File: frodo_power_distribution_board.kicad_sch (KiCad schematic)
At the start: 3 parts, among them J1 Payload_1, J2 Payload_2, J3 Payload_3

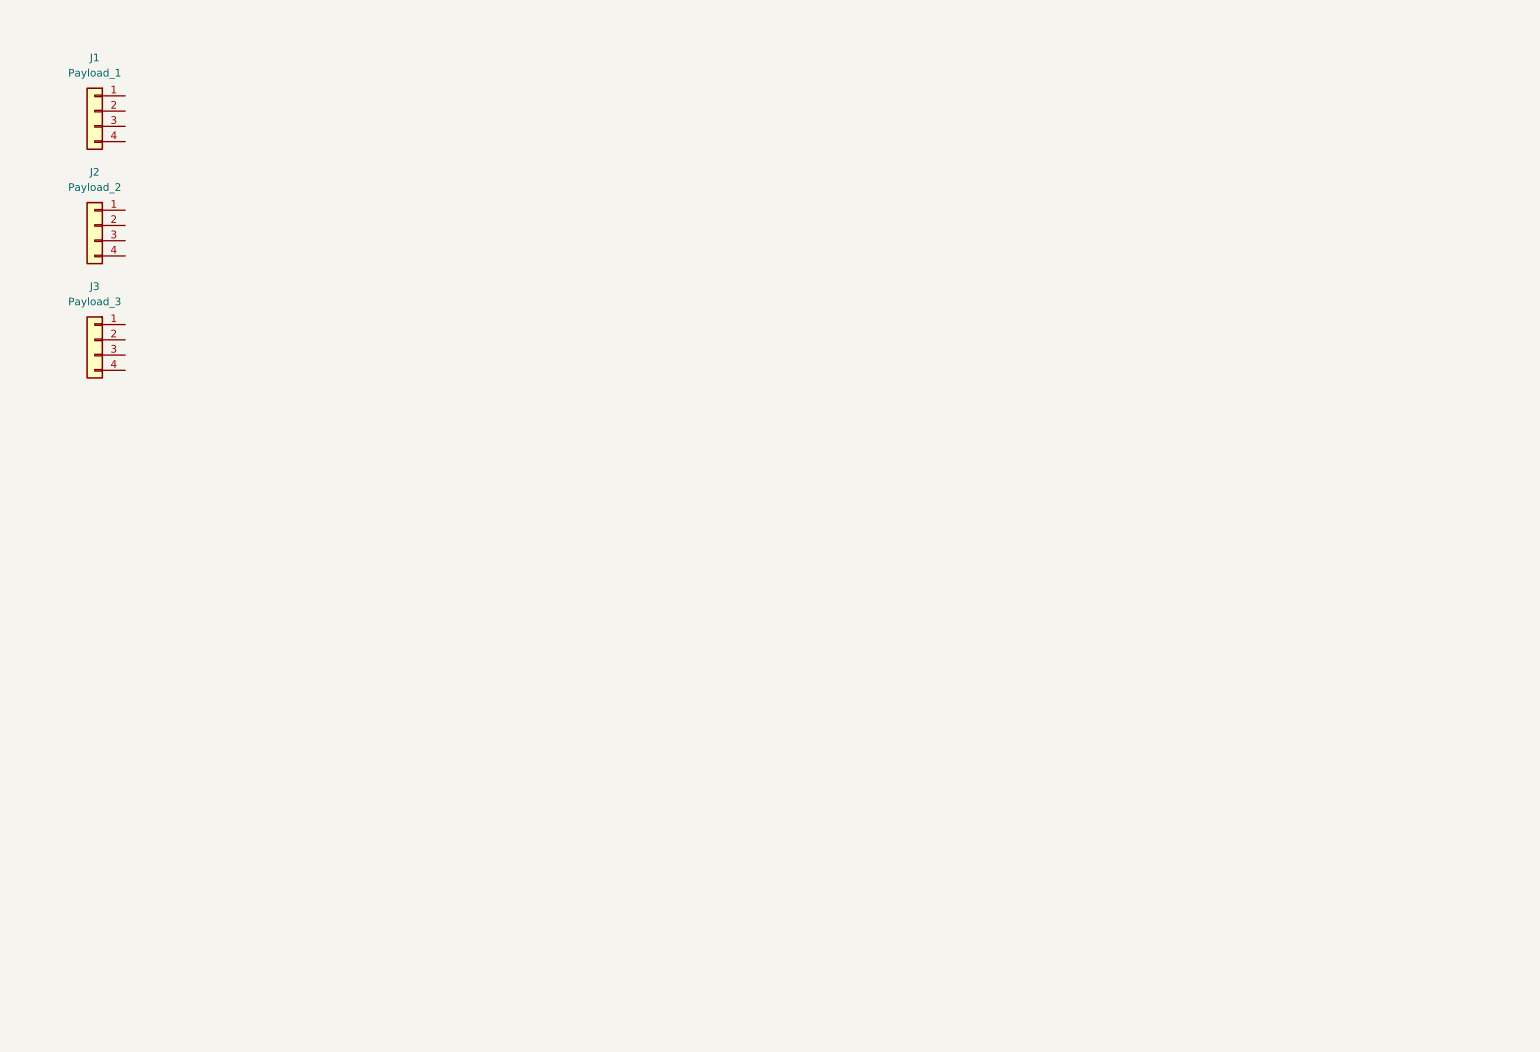
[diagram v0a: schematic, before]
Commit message: Specify board schematics
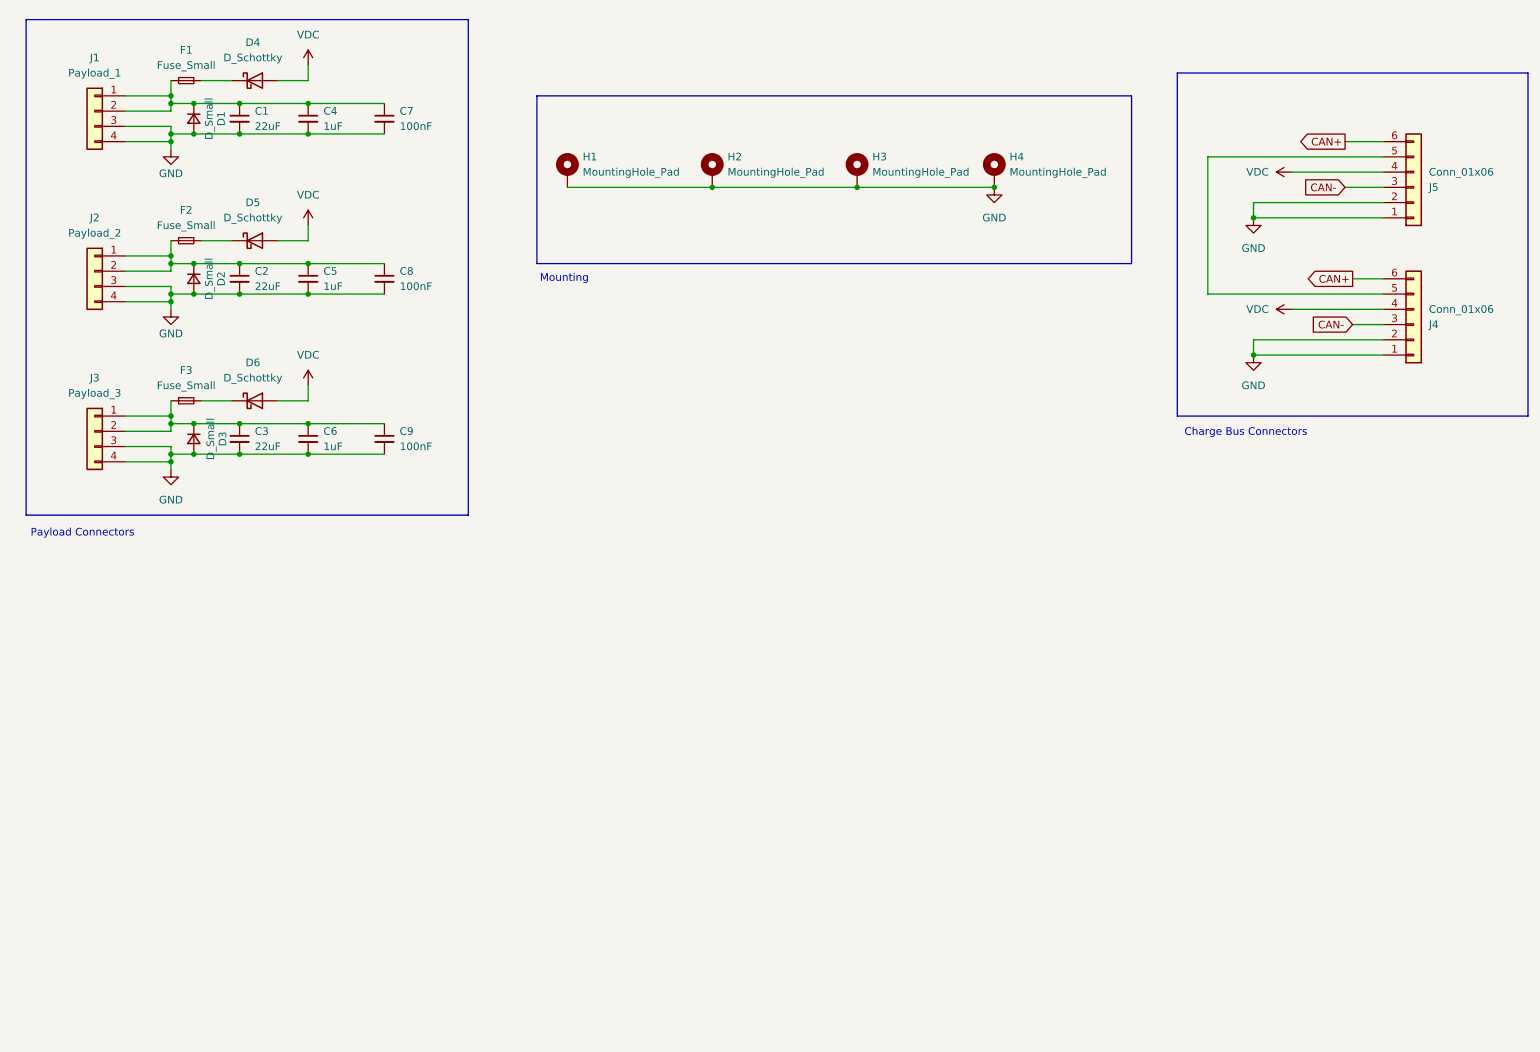
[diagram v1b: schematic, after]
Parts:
- added C1, C2, C3: 22uF, Capacitor_SMD:C_1206_3216Metric_Pad1.33x1.80mm_HandSolder, symbol Device:C_Small
- added C4, C5, C6: 1uF, Capacitor_SMD:C_0805_2012Metric_Pad1.18x1.45mm_HandSolder, symbol Device:C_Small
- added C7, C8, C9: 100nF, Capacitor_SMD:C_0603_1608Metric_Pad1.08x0.95mm_HandSolder, symbol Device:C_Small
- added D1, D2, D3: D_Small, Diode_SMD:D_SOD-123F, symbol Device:D_Small
- added D4, D5, D6: D_Schottky, Diode_SMD:D_SMA, symbol Device:D_Schottky
- added F1, F2, F3: Fuse_Small, Fuse:Fuse_1206_3216Metric, symbol Device:Fuse_Small
- added H1, H2, H3, H4: MountingHole_Pad, MountingHole:MountingHole_3.2mm_M3_Pad_Via, symbol Mechanical:MountingHole_Pad
- added J4, J5: Conn_01x06, Connector_Molex:Molex_Micro-Fit_3.0_43045-0600_2x03_P3.00mm_Horizontal, symbol Connector_Generic:Conn_01x06
- J1, J2, J3: footprint (none) -> Connector_Molex:Molex_Micro-Fit_3.0_43045-0400_2x02_P3.00mm_Horizontal
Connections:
- net at J2.1 (Pin_1): now also J2.2 (Pin_2), C2.1, C5.1, C8.1, D2.1 (K), F2.1
- net GND: now reaches J2.3 (Pin_3)
- net GND: now also J1.3 (Pin_3), J1.4 (Pin_4), J2.4 (Pin_4), J3.3 (Pin_3), J3.4 (Pin_4), C1.2, C2.2, C3.2, C4.2, C5.2, C6.2, C7.2, C8.2, C9.2, D1.2 (A), D2.2 (A), D3.2 (A), H1.1, H2.1, H3.1, H4.1, J4.1 (Pin_1), J4.2 (Pin_2), J5.1 (Pin_1), J5.2 (Pin_2)
- net at J1.1 (Pin_1): now also J1.2 (Pin_2), C1.1, C4.1, C7.1, D1.1 (K), F1.1
- net at J3.1 (Pin_1): now also J3.2 (Pin_2), C3.1, C6.1, C9.1, D3.1 (K), F3.1
- new net: J4.5 (Pin_5), J5.5 (Pin_5)
- new net: D4.1 (K), F1.2
- new net: D5.1 (K), F2.2
- new net: D6.1 (K), F3.2
- new net CAN+: J4.6 (Pin_6), J5.6 (Pin_6)
- new net CAN-: J4.3 (Pin_3), J5.3 (Pin_3)
- new net VDC: D4.2 (A), D5.2 (A), D6.2 (A), J4.4 (Pin_4), J5.4 (Pin_4)
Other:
- note added: "Charge Bus Connectors"
- note added: "Mounting"
- note added: "Payload Connectors"
- title: (none) -> Frodo Power Distribution Board
- moved on the sheet: J2, J3

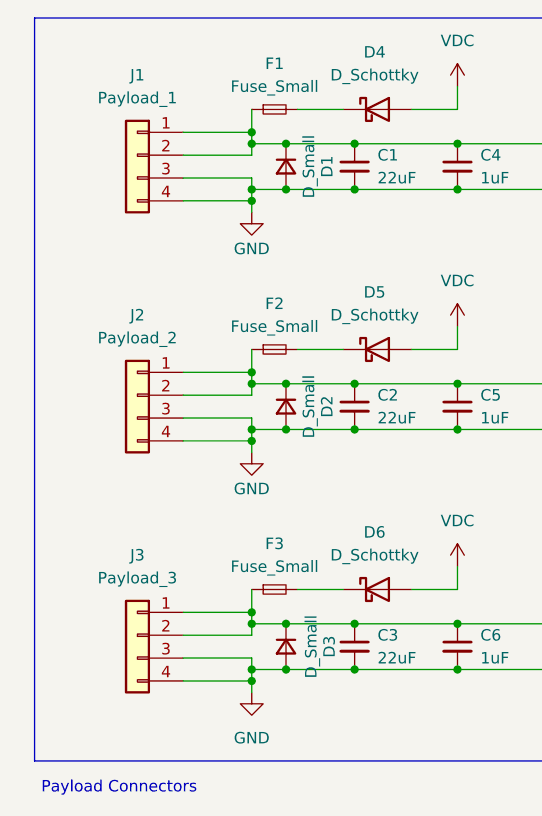
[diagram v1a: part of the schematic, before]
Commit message: Fatten traces, remove thermal relief, fix 2x2 pinout, move filter components inline
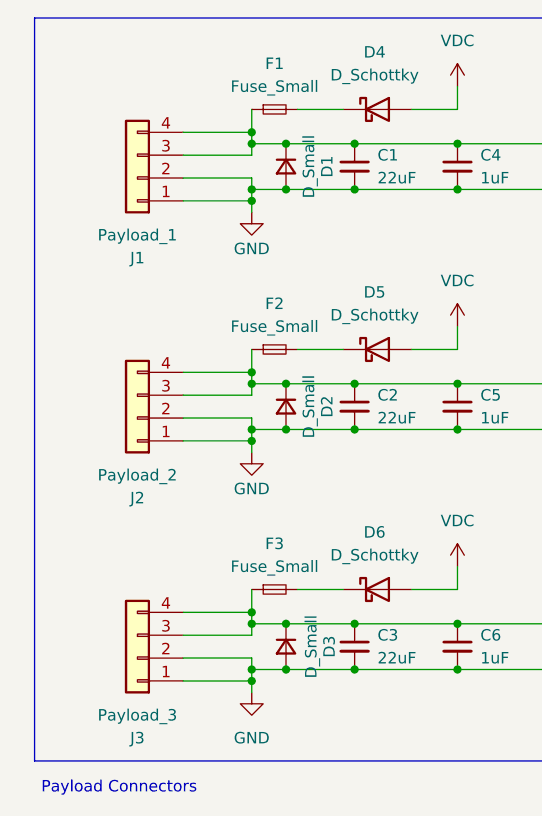
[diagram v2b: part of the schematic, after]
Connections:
- net GND: now also J1.1 (Pin_1), J1.2 (Pin_2), J2.1 (Pin_1), J2.2 (Pin_2), J3.1 (Pin_1), J3.2 (Pin_2); no longer J1.3 (Pin_3), J1.4 (Pin_4), J2.3 (Pin_3), J2.4 (Pin_4), J3.3 (Pin_3), J3.4 (Pin_4)
- net at C3.1, C6.1, C9.1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: now also J3.3 (Pin_3), J3.4 (Pin_4); no longer J3.1 (Pin_1), J3.2 (Pin_2)
- net at C2.1, C5.1, C8.1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: now also J2.3 (Pin_3), J2.4 (Pin_4); no longer J2.1 (Pin_1), J2.2 (Pin_2)
- net at C1.1, C4.1, C7.1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: now also J1.3 (Pin_3), J1.4 (Pin_4); no longer J1.1 (Pin_1), J1.2 (Pin_2)
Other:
- moved on the sheet: J1, J2, J3
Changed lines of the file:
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@@
 	(symbol
 		(lib_id "Connector_Generic:Conn_01x04")
-		(at 40.64 57.15 0)
-		(mirror y)
-		(unit 1)
-		(exclude_from_sim no)
-		(in_bom yes)
-		(on_board yes)
-		(dnp no)
-		(fields_autoplaced yes)
+		(at 40.64 59.69 180)
+		(unit 1)
+		(exclude_from_sim no)
+		(in_bom yes)
+		(on_board yes)
+		(dnp no)
 		(property "Reference" "J2"
-			(at 40.64 48.26 0)
+			(at 40.64 68.58 0)
 			(effects
 				(font
@@
 		)
 		(property "Value" "Payload_2"
-			(at 40.64 50.8 0)
+			(at 40.64 66.04 0)
 			(effects
 				(font
@@
 		)
 		(property "Footprint" "Connector_Molex:Molex_Micro-Fit_3.0_43045-0400_2x02_P3.00mm_Horizontal"
-			(at 40.64 57.15 0)
-			(effects
-				(font
-					(size 1.27 1.27)
-				)
-				(hide yes)
-			)
-		)
-		(property "Datasheet" "~"
-			(at 40.64 57.15 0)
+			(at 40.64 59.69 0)
+			(effects
+				(font
+					(size 1.27 1.27)
+				)
+				(hide yes)
+			)
+		)
+		(property "Datasheet" "~"
+			(at 40.64 59.69 0)
 			(effects
 				(font
@@
 		)
 		(property "Description" "Generic connector, single row, 01x04, script generated (kicad-library-utils/schlib/autogen/connector/)"
-			(at 40.64 57.15 0)
+			(at 40.64 59.69 0)
 			(effects
 				(font
@@
 	(symbol
 		(lib_id "Connector_Generic:Conn_01x04")
-		(at 40.64 30.48 0)
-		(mirror y)
-		(unit 1)
-		(exclude_from_sim no)
-		(in_bom yes)
-		(on_board yes)
-		(dnp no)
-		(fields_autoplaced yes)
+		(at 40.64 33.02 180)
+		(unit 1)
+		(exclude_from_sim no)
+		(in_bom yes)
+		(on_board yes)
+		(dnp no)
 		(property "Reference" "J1"
-			(at 40.64 21.59 0)
+			(at 40.64 41.91 0)
 			(effects
 				(font
@@
 		)
 		(property "Value" "Payload_1"
-			(at 40.64 24.13 0)
+			(at 40.64 39.37 0)
 			(effects
 				(font
@@
 		)
 		(property "Footprint" "Connector_Molex:Molex_Micro-Fit_3.0_43045-0400_2x02_P3.00mm_Horizontal"
-			(at 40.64 30.48 0)
-			(effects
-				(font
-					(size 1.27 1.27)
-				)
-				(hide yes)
-			)
-		)
-		(property "Datasheet" "~"
-			(at 40.64 30.48 0)
+			(at 40.64 33.02 0)
+			(effects
+				(font
+					(size 1.27 1.27)
+				)
+				(hide yes)
+			)
+		)
+		(property "Datasheet" "~"
+			(at 40.64 33.02 0)
 			(effects
 				(font
@@
 		)
 		(property "Description" "Generic connector, single row, 01x04, script generated (kicad-library-utils/schlib/autogen/connector/)"
-			(at 40.64 30.48 0)
+			(at 40.64 33.02 0)
 			(effects
 				(font
@@
 	(symbol
 		(lib_id "Connector_Generic:Conn_01x04")
-		(at 40.64 83.82 0)
-		(mirror y)
-		(unit 1)
-		(exclude_from_sim no)
-		(in_bom yes)
-		(on_board yes)
-		(dnp no)
-		(fields_autoplaced yes)
+		(at 40.64 86.36 180)
+		(unit 1)
+		(exclude_from_sim no)
+		(in_bom yes)
+		(on_board yes)
+		(dnp no)
 		(property "Reference" "J3"
-			(at 40.64 74.93 0)
+			(at 40.64 95.25 0)
 			(effects
 				(font
@@
 		)
 		(property "Value" "Payload_3"
-			(at 40.64 77.47 0)
+			(at 40.64 92.71 0)
 			(effects
 				(font
@@
 		)
 		(property "Footprint" "Connector_Molex:Molex_Micro-Fit_3.0_43045-0400_2x02_P3.00mm_Horizontal"
-			(at 40.64 83.82 0)
-			(effects
-				(font
-					(size 1.27 1.27)
-				)
-				(hide yes)
-			)
-		)
-		(property "Datasheet" "~"
-			(at 40.64 83.82 0)
+			(at 40.64 86.36 0)
+			(effects
+				(font
+					(size 1.27 1.27)
+				)
+				(hide yes)
+			)
+		)
+		(property "Datasheet" "~"
+			(at 40.64 86.36 0)
 			(effects
 				(font
@@
 		)
 		(property "Description" "Generic connector, single row, 01x04, script generated (kicad-library-utils/schlib/autogen/connector/)"
-			(at 40.64 83.82 0)
-			(effects
-				(font
+			(at 40.64 86.36 0)
+			(effects
+				(font

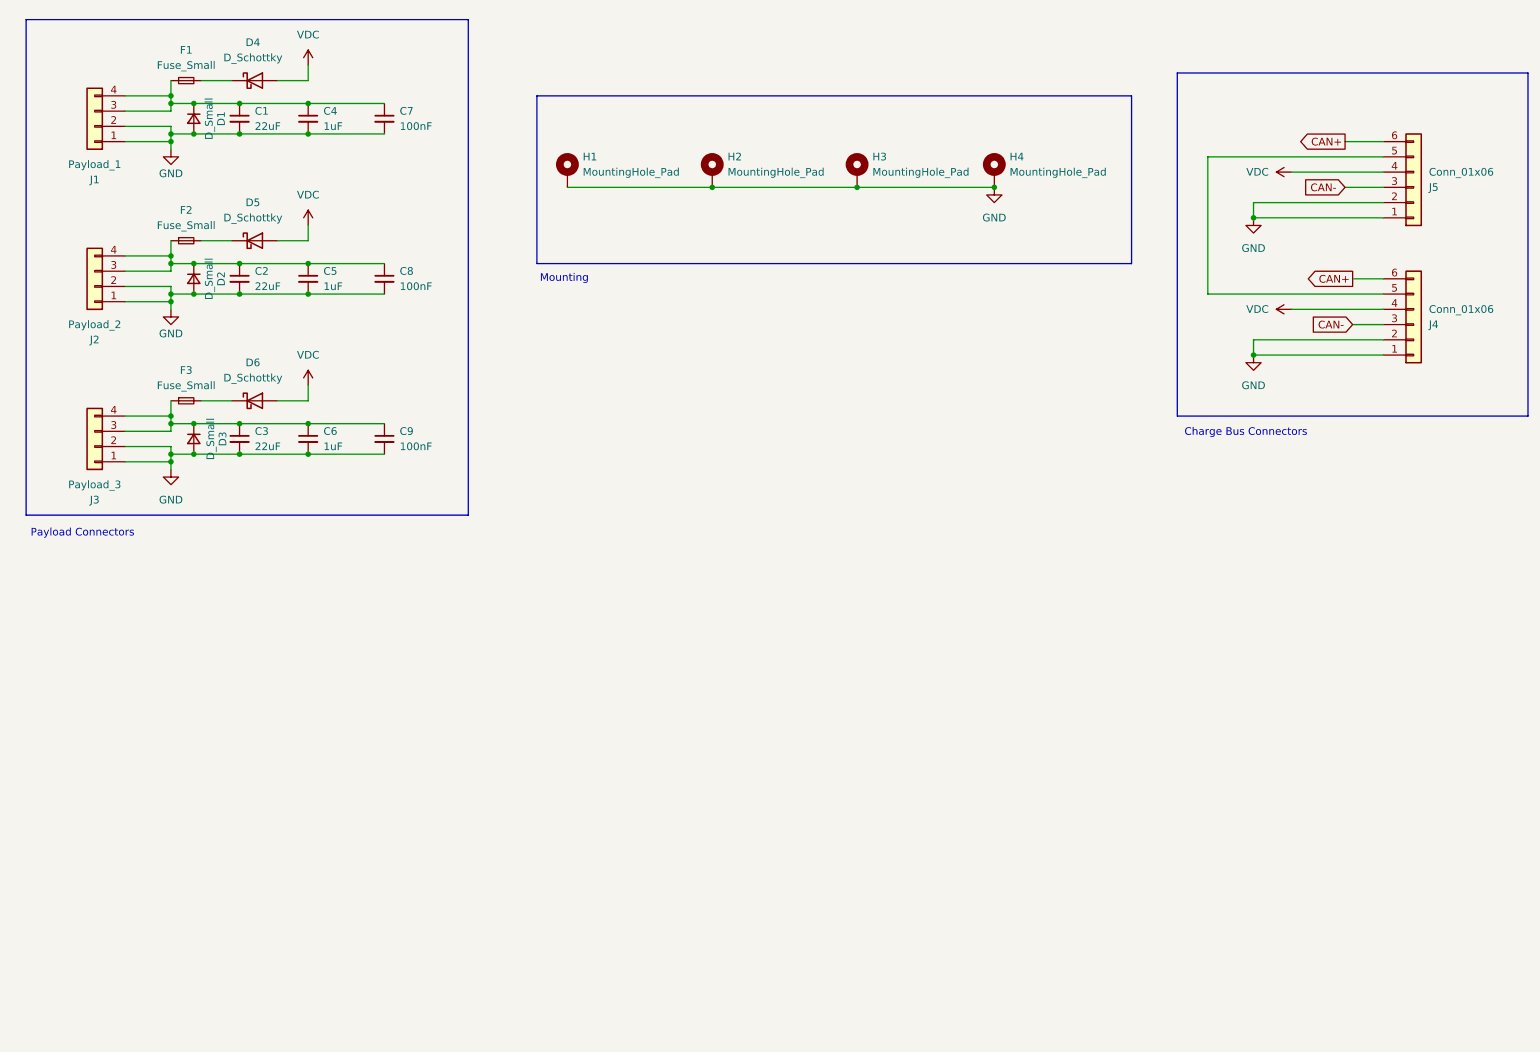
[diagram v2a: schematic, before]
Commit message: Increase number of charge bus connectors to six
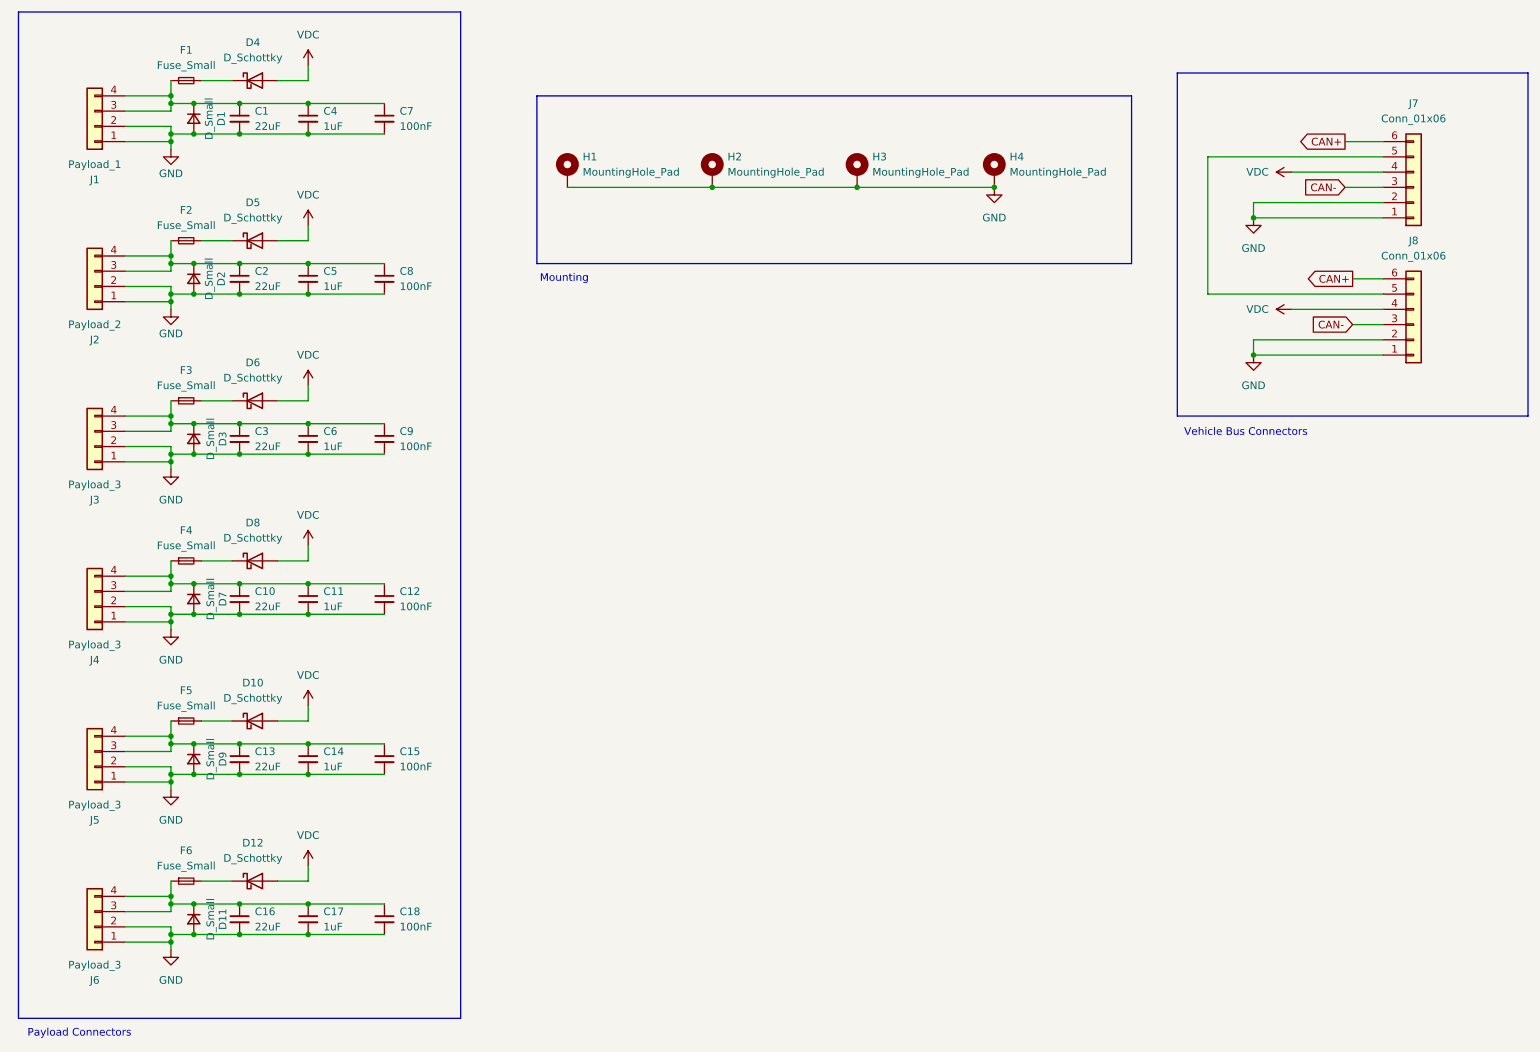
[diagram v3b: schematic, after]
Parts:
- added C10, C13, C16: 22uF, Capacitor_SMD:C_1206_3216Metric_Pad1.33x1.80mm_HandSolder, symbol Device:C_Small
- added C11, C14, C17: 1uF, Capacitor_SMD:C_0805_2012Metric_Pad1.18x1.45mm_HandSolder, symbol Device:C_Small
- added C12, C15, C18: 100nF, Capacitor_SMD:C_0603_1608Metric_Pad1.08x0.95mm_HandSolder, symbol Device:C_Small
- added D10, D12, D8: D_Schottky, Diode_SMD:D_SMA, symbol Device:D_Schottky
- added D11, D7, D9: D_Small, Diode_SMD:D_SOD-123F, symbol Device:D_Small
- added F4, F5, F6: Fuse_Small, Fuse:Fuse_1206_3216Metric, symbol Device:Fuse_Small
- added J4, J5, J6: Payload_3, Connector_Molex:Molex_Micro-Fit_3.0_43045-0400_2x02_P3.00mm_Horizontal, symbol Connector_Generic:Conn_01x04
- renumbered J5 to J7, J4 to J8
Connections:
- net GND: now also C10.2, C11.2, C12.2, C13.2, C14.2, C15.2, C16.2, C17.2, C18.2, D11.2 (A), D7.2 (A), D9.2 (A), J4.1 (Pin_1), J4.2 (Pin_2), J5.1 (Pin_1), J5.2 (Pin_2), J6.1 (Pin_1), J6.2 (Pin_2)
- net VDC: now also D10.2 (A), D12.2 (A), D8.2 (A)
- new net: C10.1, C11.1, C12.1, D7.1 (K), F4.1, J4.3 (Pin_3), J4.4 (Pin_4)
- new net: D12.1 (K), F6.2
- new net: C16.1, C17.1, C18.1, D11.1 (K), F6.1, J6.3 (Pin_3), J6.4 (Pin_4)
- new net: C13.1, C14.1, C15.1, D9.1 (K), F5.1, J5.3 (Pin_3), J5.4 (Pin_4)
- new net: D10.1 (K), F5.2
- new net: D8.1 (K), F4.2
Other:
- note added: "Vehicle Bus Connectors"
- note removed: "Charge Bus Connectors"
